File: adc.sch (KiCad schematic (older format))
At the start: 17 parts, among them U1 LM321

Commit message: addgit ignopre
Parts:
- added R?: 4.7K, Resistor_SMD:R_0805_2012Metric, symbol Device:R
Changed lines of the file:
@@
 $Descr A4 11693 8268
 encoding utf-8
-Sheet 3 4
+Sheet 2 6
 Title ""
 Date ""
@@
 	8250 2200 8300 2200
 Connection ~ 8250 2200
+$Comp
+L Device:R R?
+U 1 1 5E3754F8
+P 2850 3400
+AR Path="/5E300FCE/5E3754F8" Ref="R?"  Part="1"
+AR Path="/5E350920/5E3754F8" Ref="R?"  Part="1"
+F 0 "R?" H 2920 3446 50  0000 L CNN
+F 1 "4.7K" H 2920 3355 50  0000 L CNN
+F 2 "Resistor_SMD:R_0805_2012Metric" V 2780 3400 50  0001 C CNN
+F 3 "~" H 2850 3400 50  0001 C CNN
+F 4 "R0805" H 2920 3287 31  0000 L CNN "size"
+	1    2850 3400
+	1    0    0    -1
+$EndComp
 $EndSCHEMATC

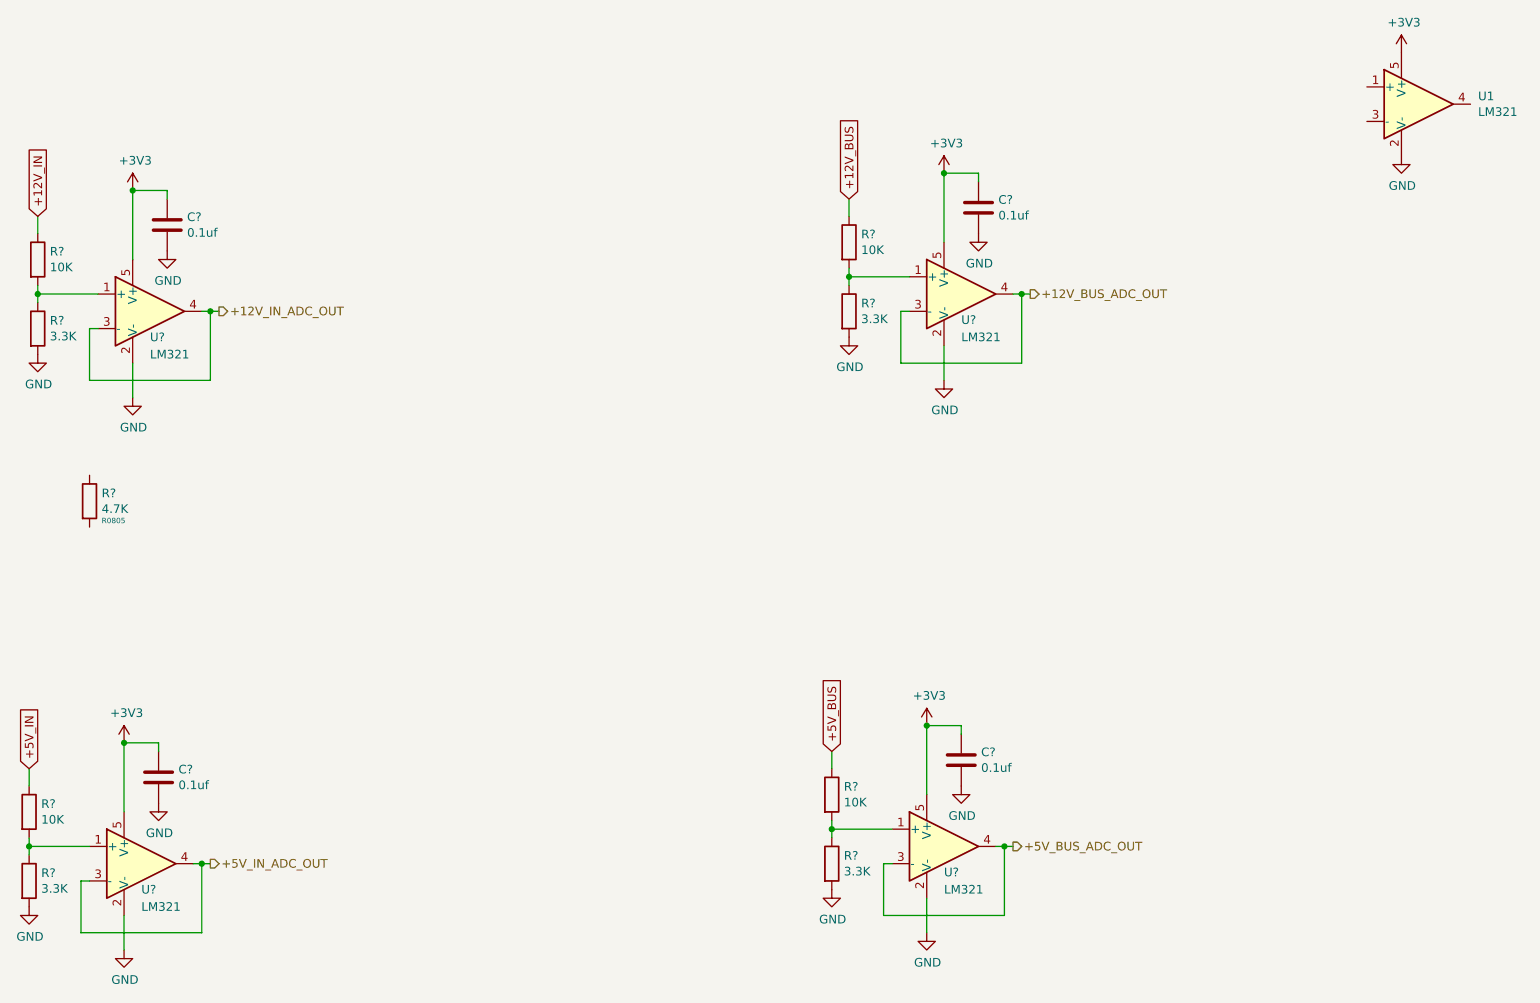
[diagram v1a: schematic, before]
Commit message: resistor symbol modify
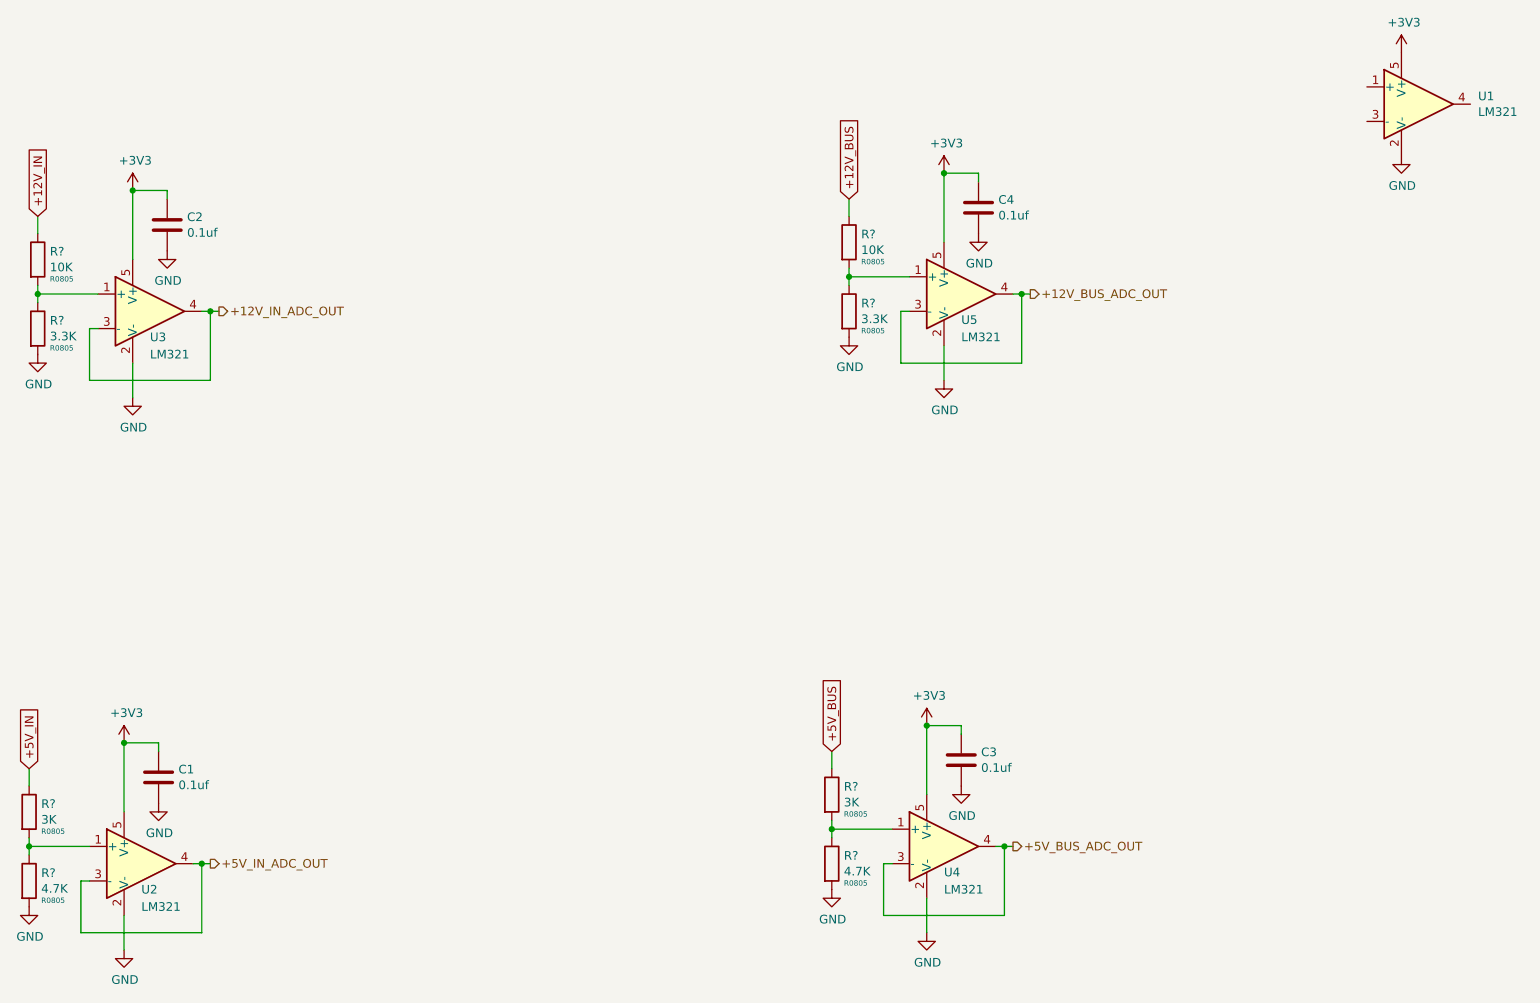
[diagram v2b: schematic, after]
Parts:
- removed R? (x4): 10K, Resistor_SMD:R_0805_2012Metric, symbol Device:R
- removed R? (x4): 3.3K, Resistor_SMD:R_0805_2012Metric, symbol Device:R
- removed R?: 4.7K, Resistor_SMD:R_0805_2012Metric, symbol Device:R
- added R? (x2): 10K, Resistor_SMD:R_0805_2012Metric, symbol Device:R
- added R? (x2): 3.3K, Resistor_SMD:R_0805_2012Metric, symbol Device:R
- added R? (x2): 3K, Resistor_SMD:R_0805_2012Metric, symbol Device:R
- added R? (x2): 4.7K, Resistor_SMD:R_0805_2012Metric, symbol Device:R
- gave numbers to parts that had none: 8
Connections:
- net +12V_BUS: now also R?.1
- net +12V_IN: now also R?.1
- net +5V_BUS: now also R?.1
- net +5V_IN: now also R?.1
- net GND: now also R?.2, R?.2, R?.2, R?.2
- net at U3.1 (+): now also R?.1, R?.2
- net at U2.1 (+): now also R?.1, R?.2
- net at U5.1 (+): now also R?.1, R?.2
- net at U4.1 (+): now also R?.1, R?.2
